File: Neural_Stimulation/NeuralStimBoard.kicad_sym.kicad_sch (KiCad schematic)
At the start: 1 part, among them U1 CSI040

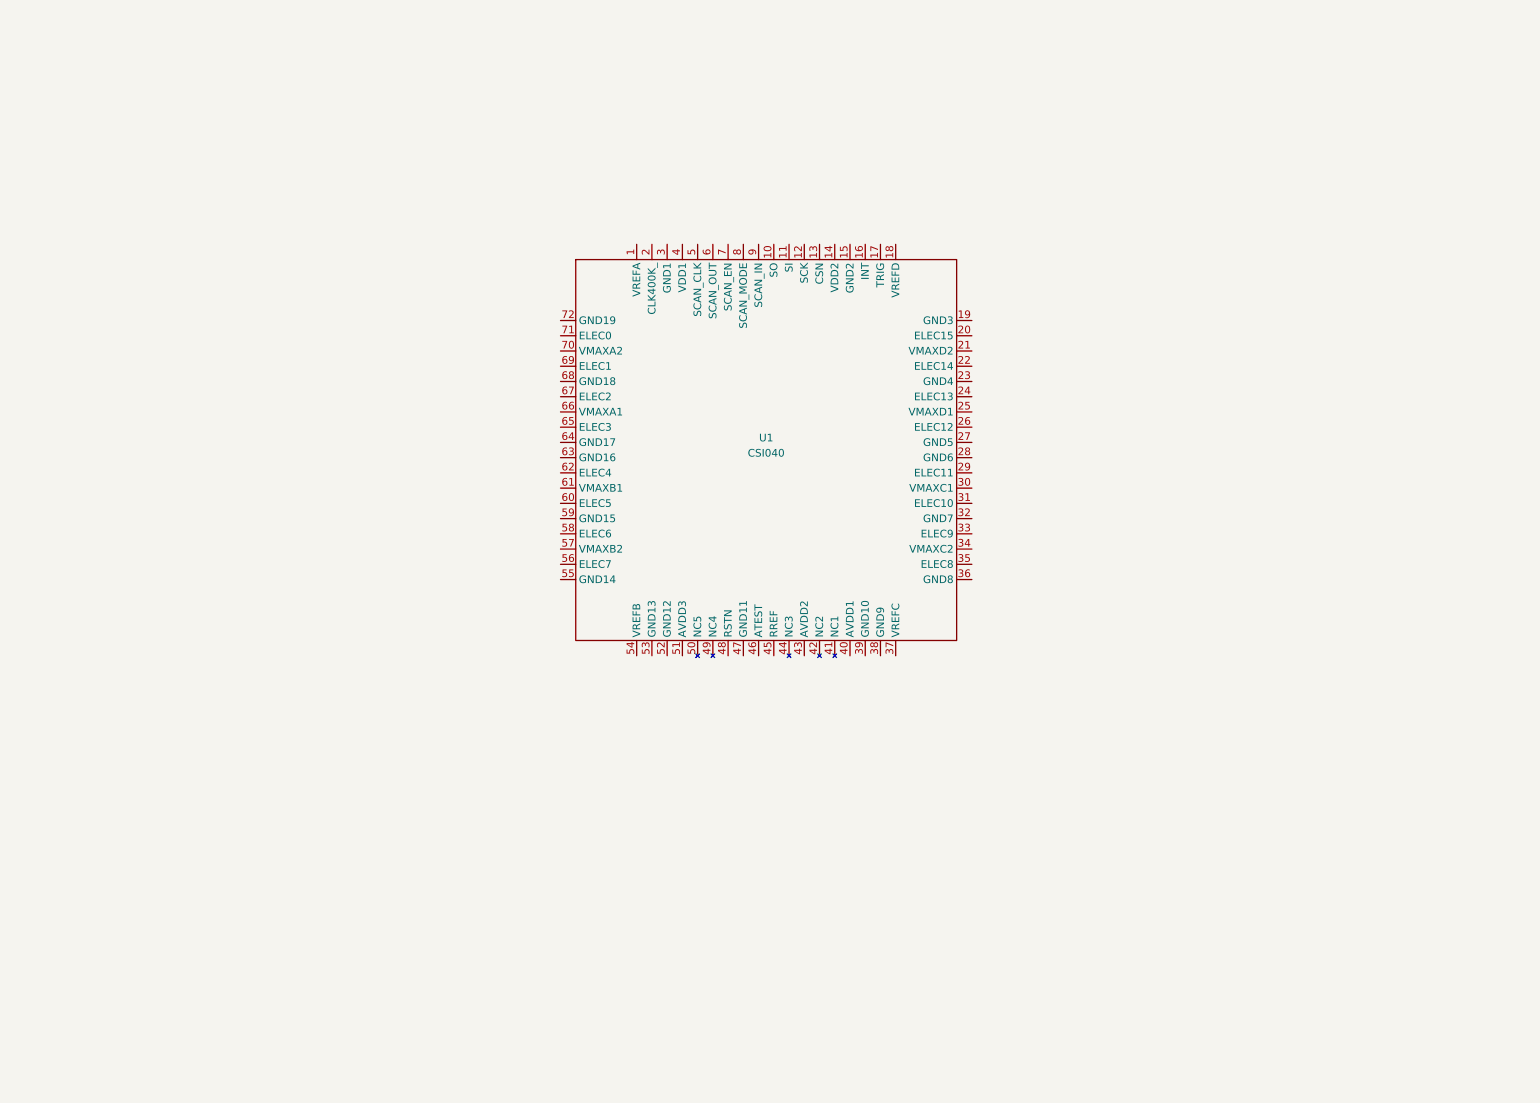
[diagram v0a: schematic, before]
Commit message: Added circuit for electrodes
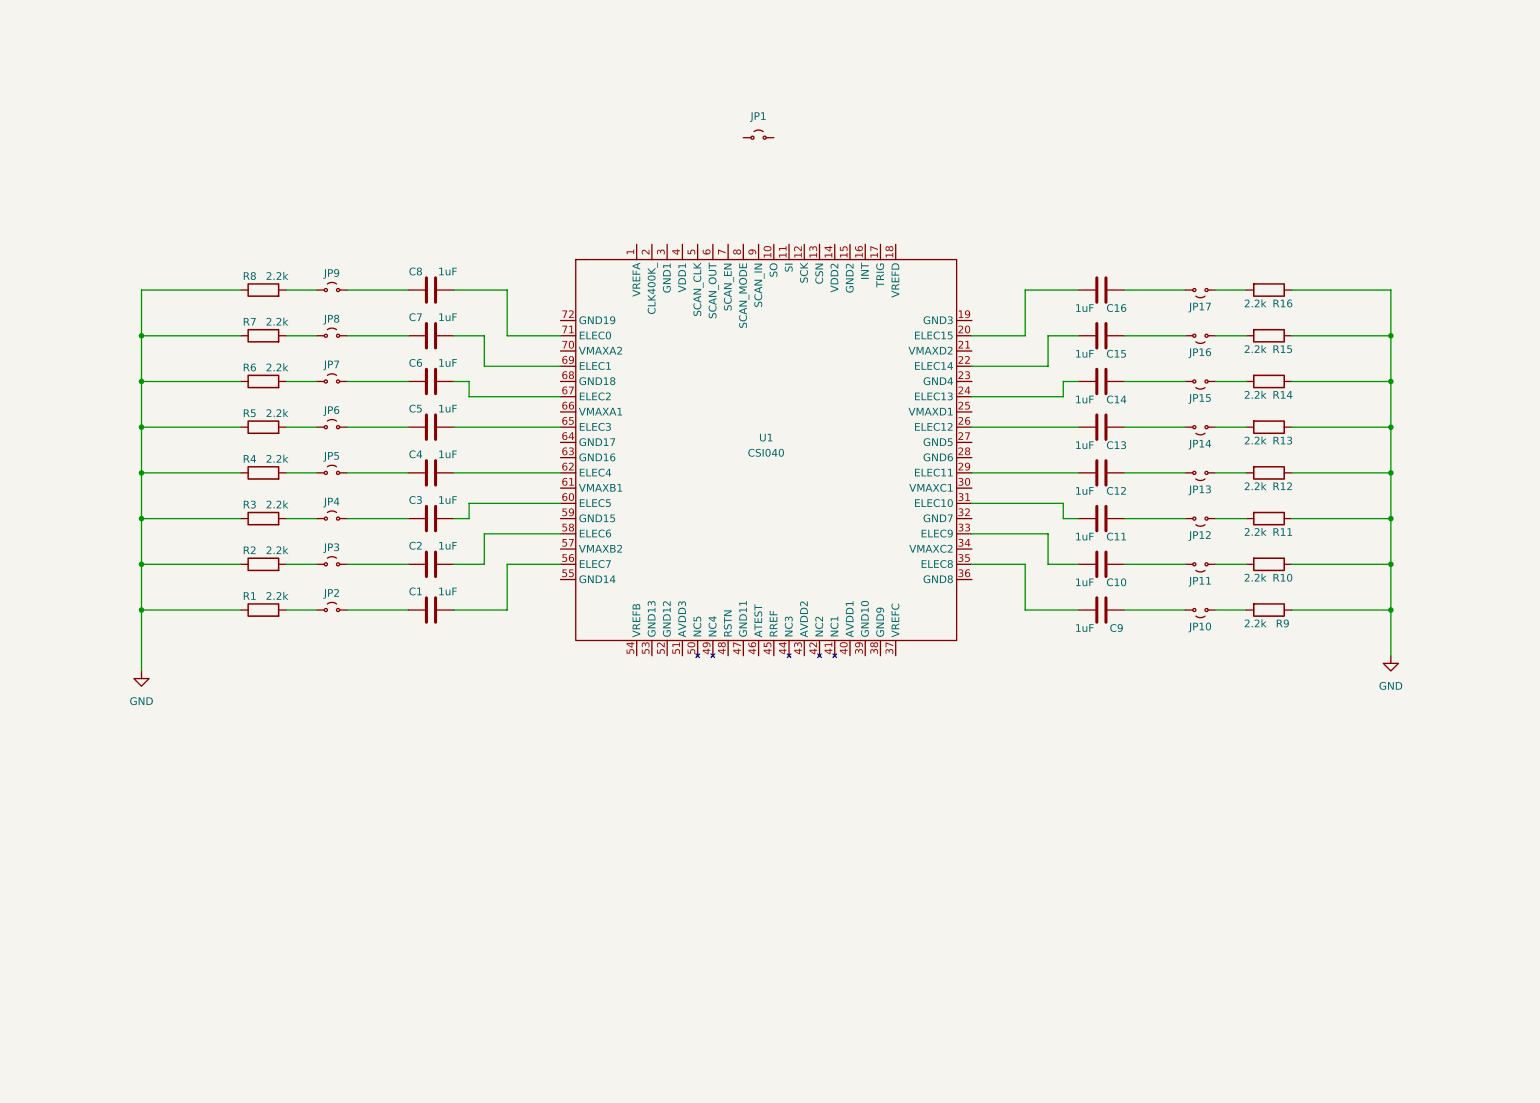
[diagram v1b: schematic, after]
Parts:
- added C1, C10, C11, C12, C13, C14, C15, C16, C2, C3, C4, C5, C6, C7, C8, C9: 1uF, symbol Device:C
- added JP1, JP10, JP11, JP12, JP13, JP14, JP15, JP16, JP17, JP2, JP3, JP4, JP5, JP6, JP7, JP8, JP9: Jumper_2_Small_Open, symbol Jumper:Jumper_2_Small_Open
- added R1, R10, R11, R12, R13, R14, R15, R16, R2, R3, R4, R5, R6, R7, R8, R9: 2.2k, symbol Device:R
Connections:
- net at U1.20 (ELEC15): now also C16.2
- net at U1.22 (ELEC14): now also C15.2
- net at U1.24 (ELEC13): now also C14.2
- net at U1.26 (ELEC12): now also C13.2
- net at U1.29 (ELEC11): now also C12.2
- net at U1.31 (ELEC10): now also C11.2
- net at U1.33 (ELEC9): now also C10.2
- net at U1.35 (ELEC8): now also C9.2
- net at U1.56 (ELEC7): now also C1.2
- net at U1.58 (ELEC6): now also C2.2
- net at U1.60 (ELEC5): now also C3.2
- net at U1.62 (ELEC4): now also C4.2
- net at U1.65 (ELEC3): now also C5.2
- net at U1.67 (ELEC2): now also C6.2
- net at U1.69 (ELEC1): now also C7.2
- net at U1.71 (ELEC0): now also C8.2
- new net: JP15.1 (A), R14.2
- new net: C14.1, JP15.2 (B)
- new net: JP8.1 (A), R7.2
- new net: JP3.1 (A), R2.2
- new net: C2.1, JP3.2 (B)
- new net: C6.1, JP7.2 (B)
- new net: JP7.1 (A), R6.2
- new net: C10.1, JP11.2 (B)
- new net: C8.1, JP9.2 (B)
- new net: JP9.1 (A), R8.2
- new net: JP4.1 (A), R3.2
- new net: C3.1, JP4.2 (B)
- new net: JP14.1 (A), R13.2
- new net: C13.1, JP14.2 (B)
- new net: C1.1, JP2.2 (B)
- new net: JP11.1 (A), R10.2
- new net: JP5.1 (A), R4.2
- new net: C4.1, JP5.2 (B)
- new net: C16.1, JP17.2 (B)
- new net: C15.1, JP16.2 (B)
- new net: C9.1, JP10.2 (B)
- new net: C7.1, JP8.2 (B)
- new net: JP10.1 (A), R9.2
- new net: JP17.1 (A), R16.2
- new net: JP6.1 (A), R5.2
- new net: C5.1, JP6.2 (B)
- new net: JP16.1 (A), R15.2
- new net: JP13.1 (A), R12.2
- new net: C12.1, JP13.2 (B)
- new net: JP12.1 (A), R11.2
- new net: JP2.1 (A), R1.2
- new net: C11.1, JP12.2 (B)
- new net GND: R1.1, R10.1, R11.1, R12.1, R13.1, R14.1, R15.1, R16.1, R2.1, R3.1, R4.1, R5.1, R6.1, R7.1, R8.1, R9.1

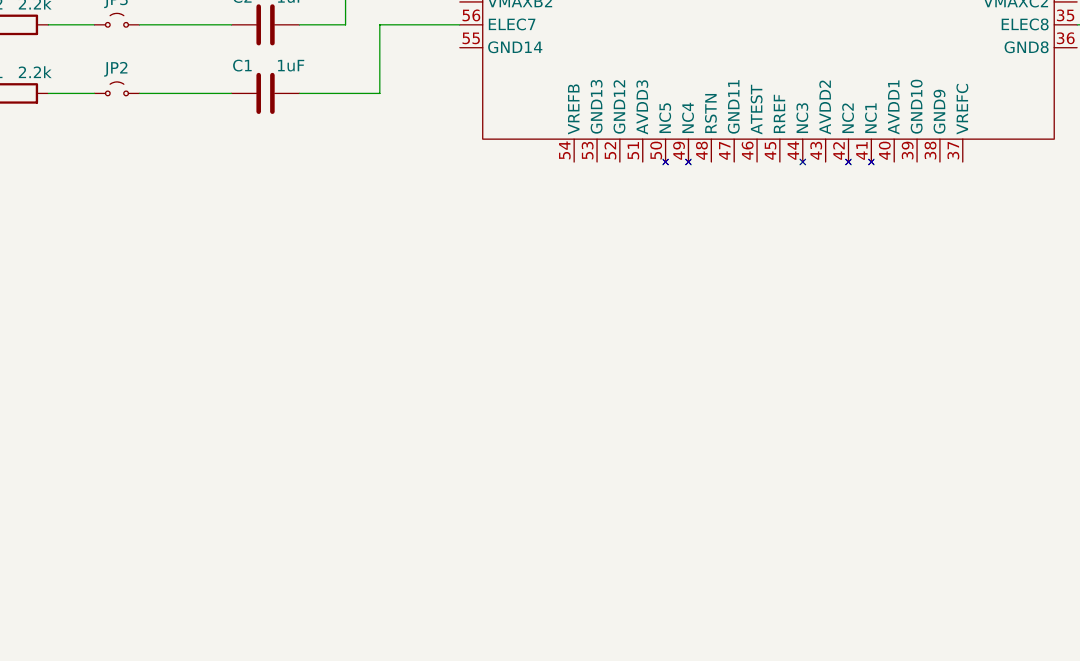
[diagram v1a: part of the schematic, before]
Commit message: Added Adafruit Feather ESP32S3 Custom symbol
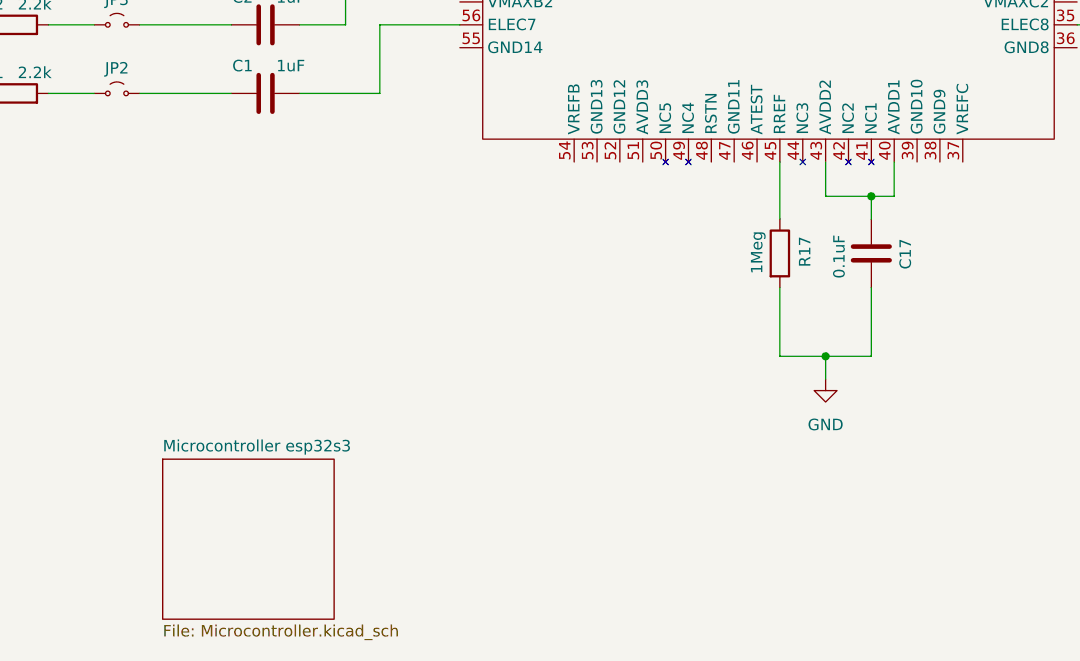
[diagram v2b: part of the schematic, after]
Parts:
- added C17: 0.1uF, symbol Device:C
- added R17: 1Meg, symbol Device:R
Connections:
- net GND: now also C17.2, R17.2
- net at U1.40 (AVDD1): now also U1.43 (AVDD2), C17.1
- net at U1.45 (RREF): now also R17.1
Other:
- added sheet Microcontroller esp32s3 (Microcontroller.kicad_sch)

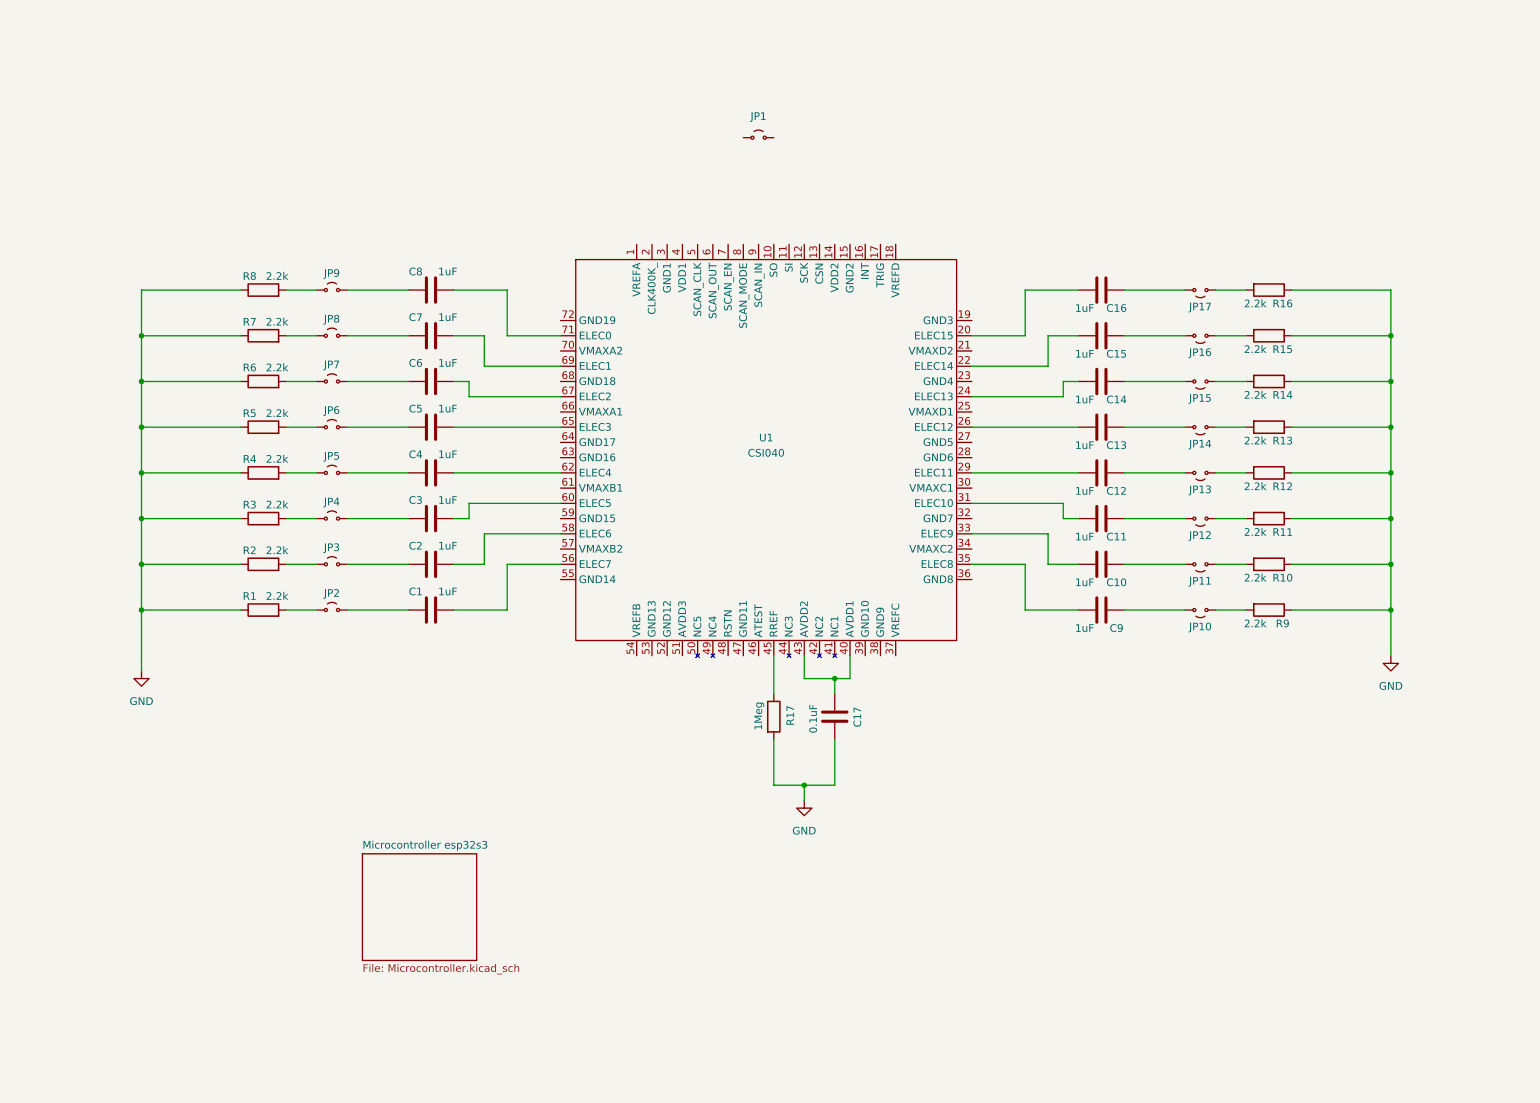
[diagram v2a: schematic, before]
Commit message: Added LDO
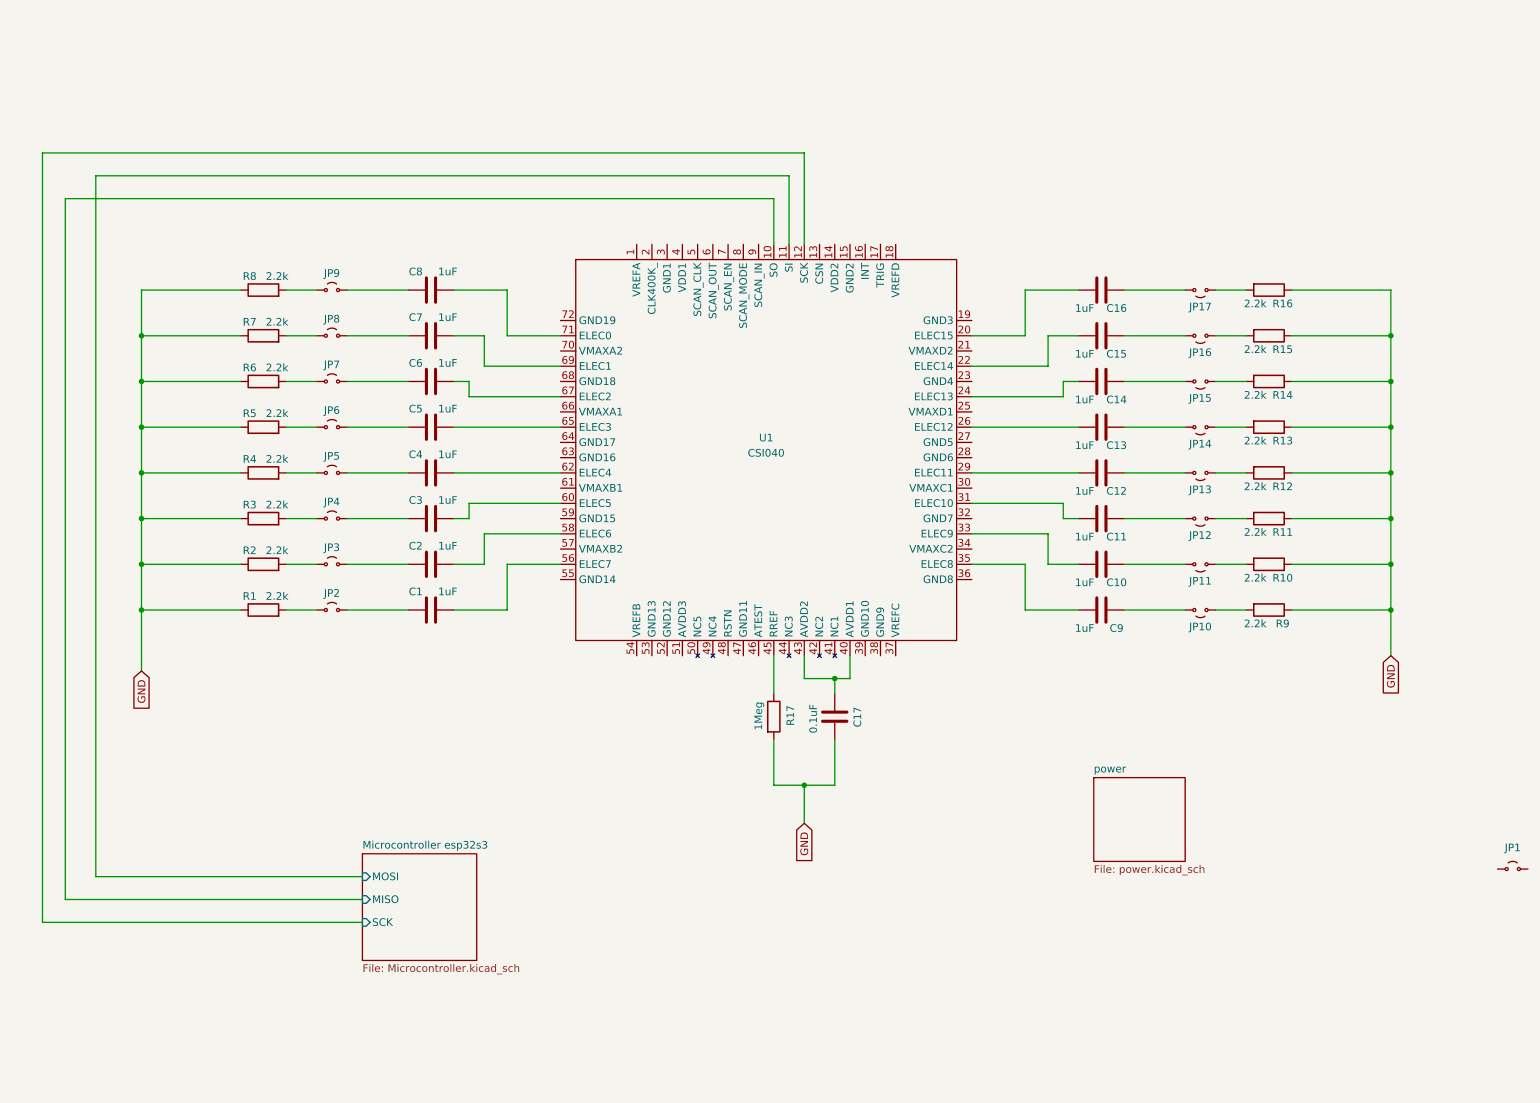
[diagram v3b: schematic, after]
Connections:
- net Microcontroller esp32s3/MISO: now reaches U1.10 (SO)
- net Microcontroller esp32s3/MOSI: now reaches U1.11 (SI)
- net Microcontroller esp32s3/SCK: now reaches U1.12 (SCK)
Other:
- added sheet power (power.kicad_sch)
- sheet Microcontroller esp32s3 ports: added MISO, MOSI, SCK; removed none
- moved on the sheet: JP1
